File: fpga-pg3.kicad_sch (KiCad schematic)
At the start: 20 parts, among them U1 XC7A35T-FGG484

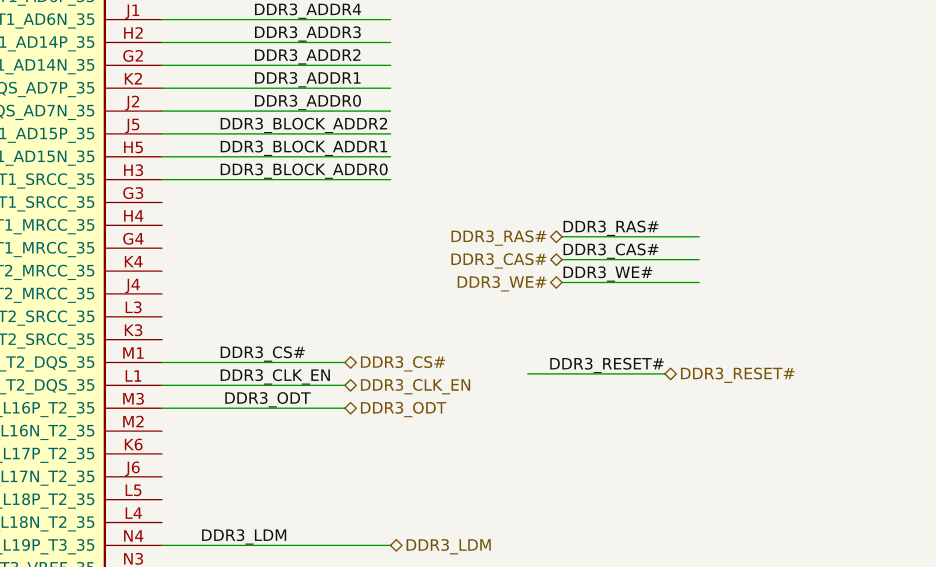
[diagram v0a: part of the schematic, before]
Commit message: filled out back connector, finished ddr pinning according to vivado
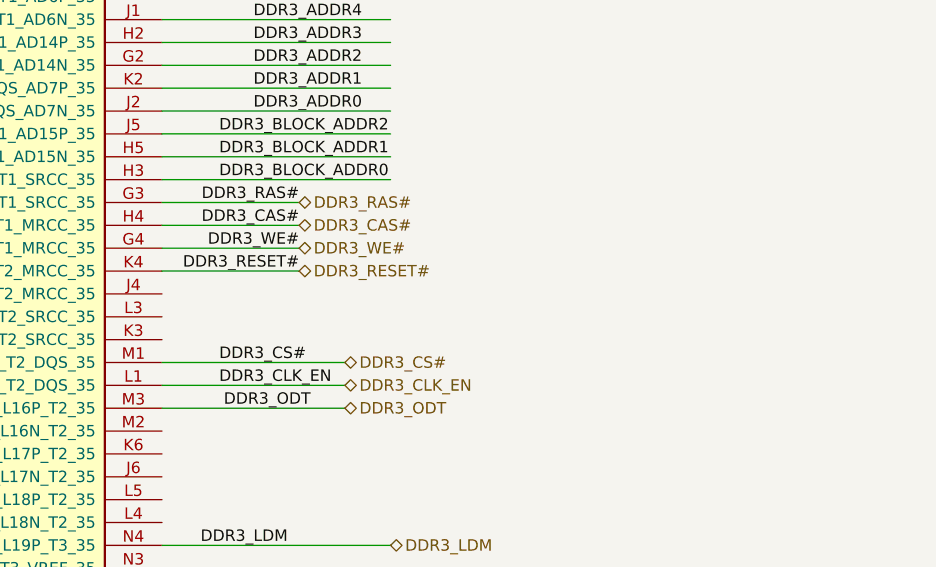
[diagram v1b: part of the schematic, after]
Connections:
- net DDR3_CAS#: now also U1.H4 (IO_L12P_T1_MRCC_35)
- net DDR3_RAS#: now also U1.G3 (IO_L11N_T1_SRCC_35)
- net DDR3_RESET#: now also U1.K4 (IO_L13P_T2_MRCC_35)
- net DDR3_WE#: now also U1.G4 (IO_L12N_T1_MRCC_35)
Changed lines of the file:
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@@
 	(wire
 		(pts
-			(xy 299.72 146.05) (xy 314.96 146.05)
+			(xy 270.51 142.24) (xy 255.27 142.24)
 		)
 		(stroke
@@
 	(wire
 		(pts
-			(xy 299.72 148.59) (xy 314.96 148.59)
-		)
-		(stroke
-			(width 0)
-			(type default)
-		)
-	)
-	(wire
-		(pts
-			(xy 299.72 151.13) (xy 314.96 151.13)
+			(xy 270.51 144.78) (xy 255.27 144.78)
+		)
+		(stroke
+			(width 0)
+			(type default)
+		)
+	)
+	(wire
+		(pts
+			(xy 270.51 147.32) (xy 255.27 147.32)
 		)
 		(stroke
@@
 	(wire
 		(pts
-			(xy 311.15 161.29) (xy 295.91 161.29)
+			(xy 270.51 149.86) (xy 255.27 149.86)
 		)
 		(stroke
@@
 	)
 	(label "DDR3_RAS#"
-		(at 299.72 146.05 0)
-		(effects
-			(font
-				(size 1.27 1.27)
-			)
-			(justify left bottom)
+		(at 270.51 142.24 180)
+		(effects
+			(font
+				(size 1.27 1.27)
+			)
+			(justify right bottom)
 		)
 	)
@@
 	)
 	(label "DDR3_WE#"
-		(at 299.72 151.13 0)
-		(effects
-			(font
-				(size 1.27 1.27)
-			)
-			(justify left bottom)
+		(at 270.51 147.32 180)
+		(effects
+			(font
+				(size 1.27 1.27)
+			)
+			(justify right bottom)
 		)
 	)
@@
 	)
 	(label "DDR3_CAS#"
-		(at 299.72 148.59 0)
-		(effects
-			(font
-				(size 1.27 1.27)
-			)
-			(justify left bottom)
+		(at 270.51 144.78 180)
+		(effects
+			(font
+				(size 1.27 1.27)
+			)
+			(justify right bottom)
 		)
 	)
@@
 	)
 	(label "DDR3_RESET#"
-		(at 311.15 161.29 180)
+		(at 270.51 149.86 180)
 		(effects
 			(font
@@
 	(hierarchical_label "DDR3_RESET#"
 		(shape bidirectional)
-		(at 311.15 161.29 0)
+		(at 270.51 149.86 0)
 		(effects
 			(font
@@
 	(hierarchical_label "DDR3_WE#"
 		(shape bidirectional)
-		(at 299.72 151.13 180)
-		(effects
-			(font
-				(size 1.27 1.27)
-			)
-			(justify right)
+		(at 270.51 147.32 0)
+		(effects
+			(font
+				(size 1.27 1.27)
+			)
+			(justify left)
 		)
 	)
@@
 	(hierarchical_label "DDR3_CAS#"
 		(shape bidirectional)
-		(at 299.72 148.59 180)
-		(effects
-			(font
-				(size 1.27 1.27)
-			)
-			(justify right)
+		(at 270.51 144.78 0)
+		(effects
+			(font
+				(size 1.27 1.27)
+			)
+			(justify left)
 		)
 	)
 	(hierarchical_label "DDR3_RAS#"
 		(shape bidirectional)
-		(at 299.72 146.05 180)
-		(effects
-			(font
-				(size 1.27 1.27)
-			)
-			(justify right)
-		)
-	)
+		(at 270.51 142.24 0)
+		(effects
+			(font
+				(size 1.27 1.27)
+			)
+			(justify left)
+		)
+	)

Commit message: added a lot of stuff
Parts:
- renumbered C72 to C29, C73 to C30, C74 to C31, C75 to C32, C76 to C33, C77 to C34, C78 to C35, C79 to C36, C80 to C37, C81 to C38, C82 to C39, C83 to C40, C84 to C41, C85 to C42, R11 to R1, R12 to R2, R13 to R3, R14 to R4, R15 to R5
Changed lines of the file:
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@@
 		(on_board yes)
 		(dnp no)
-		(property "Reference" "C73"
+		(property "Reference" "C30"
 			(at 91.44 52.0699 0)
 			(effects
@@
 			(project "logix-core"
 				(path "/cf3b7c5f-6ddc-4e3f-9529-0bcf5eec6f23/824409ff-e0aa-4944-ad80-228eadb659f9/9208eeea-aa23-4f0a-a0f4-52abaf751fbe"
-					(reference "C73")
+					(reference "C30")
 					(unit 1)
 				)
@@
 		(dnp no)
 		(fields_autoplaced yes)
-		(property "Reference" "C78"
+		(property "Reference" "C35"
 			(at 154.94 52.0699 0)
 			(effects
@@
 			(project "logix-core"
 				(path "/cf3b7c5f-6ddc-4e3f-9529-0bcf5eec6f23/824409ff-e0aa-4944-ad80-228eadb659f9/9208eeea-aa23-4f0a-a0f4-52abaf751fbe"
-					(reference "C78")
+					(reference "C35")
 					(unit 1)
 				)
@@
 		(dnp no)
 		(fields_autoplaced yes)
-		(property "Reference" "C75"
+		(property "Reference" "C32"
 			(at 116.84 52.0699 0)
 			(effects
@@
 			(project "logix-core"
 				(path "/cf3b7c5f-6ddc-4e3f-9529-0bcf5eec6f23/824409ff-e0aa-4944-ad80-228eadb659f9/9208eeea-aa23-4f0a-a0f4-52abaf751fbe"
-					(reference "C75")
+					(reference "C32")
 					(unit 1)
 				)
@@
 		(on_board yes)
 		(dnp no)
-		(property "Reference" "R15"
+		(property "Reference" "R5"
 			(at -90.424 94.488 90)
 			(effects
@@
 			(project "logix-core"
 				(path "/cf3b7c5f-6ddc-4e3f-9529-0bcf5eec6f23/824409ff-e0aa-4944-ad80-228eadb659f9/9208eeea-aa23-4f0a-a0f4-52abaf751fbe"
-					(reference "R15")
+					(reference "R5")
 					(unit 1)
 				)
@@
 		(on_board yes)
 		(dnp no)
-		(property "Reference" "R11"
+		(property "Reference" "R1"
 			(at -90.424 69.088 90)
 			(effects
@@
 			(project "logix-core"
 				(path "/cf3b7c5f-6ddc-4e3f-9529-0bcf5eec6f23/824409ff-e0aa-4944-ad80-228eadb659f9/9208eeea-aa23-4f0a-a0f4-52abaf751fbe"
-					(reference "R11")
+					(reference "R1")
 					(unit 1)
 				)
@@
 		(on_board yes)
 		(dnp no)
-		(property "Reference" "R13"
+		(property "Reference" "R3"
 			(at -90.424 74.168 90)
 			(effects
@@
 			(project "logix-core"
 				(path "/cf3b7c5f-6ddc-4e3f-9529-0bcf5eec6f23/824409ff-e0aa-4944-ad80-228eadb659f9/9208eeea-aa23-4f0a-a0f4-52abaf751fbe"
-					(reference "R13")
+					(reference "R3")
 					(unit 1)
 				)
@@
 		(on_board yes)
 		(dnp no)
-		(property "Reference" "R14"
+		(property "Reference" "R4"
 			(at -90.424 76.708 90)
 			(effects
@@
 			(project "logix-core"
 				(path "/cf3b7c5f-6ddc-4e3f-9529-0bcf5eec6f23/824409ff-e0aa-4944-ad80-228eadb659f9/9208eeea-aa23-4f0a-a0f4-52abaf751fbe"
-					(reference "R14")
+					(reference "R4")
 					(unit 1)
 				)
@@
 		(dnp no)
 		(fields_autoplaced yes)
-		(property "Reference" "C76"
+		(property "Reference" "C33"
 			(at 129.54 52.0699 0)
 			(effects
@@
 			(project "logix-core"
 				(path "/cf3b7c5f-6ddc-4e3f-9529-0bcf5eec6f23/824409ff-e0aa-4944-ad80-228eadb659f9/9208eeea-aa23-4f0a-a0f4-52abaf751fbe"
-					(reference "C76")
+					(reference "C33")
 					(unit 1)
 				)
@@
 		(dnp no)
 		(fields_autoplaced yes)
-		(property "Reference" "C77"
+		(property "Reference" "C34"
 			(at 142.24 52.0699 0)
 			(effects
@@
 			(project "logix-core"
 				(path "/cf3b7c5f-6ddc-4e3f-9529-0bcf5eec6f23/824409ff-e0aa-4944-ad80-228eadb659f9/9208eeea-aa23-4f0a-a0f4-52abaf751fbe"
-					(reference "C77")
+					(reference "C34")
 					(unit 1)
 				)
@@
 		(dnp no)
 		(fields_autoplaced yes)
-		(property "Reference" "#PWR071"
+		(property "Reference" "#PWR06"
 			(at 327.66 68.58 0)
 			(effects
@@
 			(project "logix-core"
 				(path "/cf3b7c5f-6ddc-4e3f-9529-0bcf5eec6f23/824409ff-e0aa-4944-ad80-228eadb659f9/9208eeea-aa23-4f0a-a0f4-52abaf751fbe"
-					(reference "#PWR071")
+					(reference "#PWR06")
 					(unit 1)
 				)
@@
 		(on_board yes)
 		(dnp no)
-		(property "Reference" "C84"
+		(property "Reference" "C41"
 			(at 317.5 52.0699 0)
 			(effects
@@
 			(project "logix-core"
 				(path "/cf3b7c5f-6ddc-4e3f-9529-0bcf5eec6f23/824409ff-e0aa-4944-ad80-228eadb659f9/9208eeea-aa23-4f0a-a0f4-52abaf751fbe"
-					(reference "C84")
+					(reference "C41")
 					(unit 1)
 				)
@@
 		(dnp no)
 		(fields_autoplaced yes)
-		(property "Reference" "C82"
+		(property "Reference" "C39"
 			(at 292.1 52.0699 0)
 			(effects
@@
 			(project "logix-core"
 				(path "/cf3b7c5f-6ddc-4e3f-9529-0bcf5eec6f23/824409ff-e0aa-4944-ad80-228eadb659f9/9208eeea-aa23-4f0a-a0f4-52abaf751fbe"
-					(reference "C82")
+					(reference "C39")
 					(unit 1)
 				)
@@
 		(dnp no)
 		(fields_autoplaced yes)
-		(property "Reference" "#PWR070"
+		(property "Reference" "#PWR05"
 			(at 81.28 68.58 0)
 			(effects
@@
 			(project "logix-core"
 				(path "/cf3b7c5f-6ddc-4e3f-9529-0bcf5eec6f23/824409ff-e0aa-4944-ad80-228eadb659f9/9208eeea-aa23-4f0a-a0f4-52abaf751fbe"
-					(reference "#PWR070")
+					(reference "#PWR05")
 					(unit 1)
 				)
@@
 		(dnp no)
 		(fields_autoplaced yes)
-		(property "Reference" "C80"
+		(property "Reference" "C37"
 			(at 266.7 52.0699 0)
 			(effects
@@
 			(project "logix-core"
 				(path "/cf3b7c5f-6ddc-4e3f-9529-0bcf5eec6f23/824409ff-e0aa-4944-ad80-228eadb659f9/9208eeea-aa23-4f0a-a0f4-52abaf751fbe"
-					(reference "C80")
+					(reference "C37")
 					(unit 1)
 				)
@@
 		(dnp no)
 		(fields_autoplaced yes)
-		(property "Reference" "C85"
+		(property "Reference" "C42"
 			(at 330.2 52.0699 0)
 			(effects
@@
 			(project "logix-core"
 				(path "/cf3b7c5f-6ddc-4e3f-9529-0bcf5eec6f23/824409ff-e0aa-4944-ad80-228eadb659f9/9208eeea-aa23-4f0a-a0f4-52abaf751fbe"
-					(reference "C85")
+					(reference "C42")
 					(unit 1)
 				)
@@
 		(dnp no)
 		(fields_autoplaced yes)
-		(property "Reference" "C74"
+		(property "Reference" "C31"
 			(at 104.14 52.0699 0)
 			(effects
@@
 			(project "logix-core"
 				(path "/cf3b7c5f-6ddc-4e3f-9529-0bcf5eec6f23/824409ff-e0aa-4944-ad80-228eadb659f9/9208eeea-aa23-4f0a-a0f4-52abaf751fbe"
-					(reference "C74")
+					(reference "C31")
 					(unit 1)
 				)
@@
 		(dnp no)
 		(fields_autoplaced yes)
-		(property "Reference" "C83"
+		(property "Reference" "C40"
 			(at 304.8 52.0699 0)
 			(effects
@@
 			(project "logix-core"
 				(path "/cf3b7c5f-6ddc-4e3f-9529-0bcf5eec6f23/824409ff-e0aa-4944-ad80-228eadb659f9/9208eeea-aa23-4f0a-a0f4-52abaf751fbe"
-					(reference "C83")
+					(reference "C40")
 					(unit 1)
 				)
@@
 		(dnp no)
 		(fields_autoplaced yes)
-		(property "Reference" "C79"
+		(property "Reference" "C36"
 			(at 254 52.0699 0)
 			(effects
@@
 			(project "logix-core"
 				(path "/cf3b7c5f-6ddc-4e3f-9529-0bcf5eec6f23/824409ff-e0aa-4944-ad80-228eadb659f9/9208eeea-aa23-4f0a-a0f4-52abaf751fbe"
-					(reference "C79")
+					(reference "C36")
 					(unit 1)
 				)
@@
 		(dnp no)
 		(fields_autoplaced yes)
-		(property "Reference" "C81"
+		(property "Reference" "C38"
 			(at 279.4 52.0699 0)
 			(effects
@@
 			(project "logix-core"
 				(path "/cf3b7c5f-6ddc-4e3f-9529-0bcf5eec6f23/824409ff-e0aa-4944-ad80-228eadb659f9/9208eeea-aa23-4f0a-a0f4-52abaf751fbe"
-					(reference "C81")
+					(reference "C38")
 					(unit 1)
 				)
@@
 		(dnp no)
 		(fields_autoplaced yes)
-		(property "Reference" "C72"
+		(property "Reference" "C29"
 			(at 78.74 52.0699 0)
 			(effects
@@
 			(project "logix-core"
 				(path "/cf3b7c5f-6ddc-4e3f-9529-0bcf5eec6f23/824409ff-e0aa-4944-ad80-228eadb659f9/9208eeea-aa23-4f0a-a0f4-52abaf751fbe"
-					(reference "C72")
+					(reference "C29")
 					(unit 1)
 				)
@@
 		(on_board yes)
 		(dnp no)
-		(property "Reference" "R12"
+		(property "Reference" "R2"
 			(at -90.424 71.628 90)
 			(effects
@@
 			(project "logix-core"
 				(path "/cf3b7c5f-6ddc-4e3f-9529-0bcf5eec6f23/824409ff-e0aa-4944-ad80-228eadb659f9/9208eeea-aa23-4f0a-a0f4-52abaf751fbe"
-					(reference "R12")
+					(reference "R2")
 					(unit 1)
 				)

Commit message: did alot of stuff
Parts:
- C29, C42: footprint Capacitor_SMD:C_1210_3225Metric -> Capacitor_SMD:C_1206_3216Metric; LCSC (none) -> C96123
- C30, C31, C40, C41: LCSC (none) -> C23733
- C32, C33, C34, C35, C36, C37, C38, C39: LCSC (none) -> C47339
- R1, R2, R3, R4, R5: footprint Resistor_SMD:R_0402_1005Metric_Pad0.72x0.64mm_HandSolder -> Resistor_SMD:R_0402_1005Metric; LCSC C226391 -> C17168
- U1: LCSC (none) -> C1521727
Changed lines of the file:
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@@
+			)
+		)
+		(property "LCSC" "C23733"
+			(at 87.63 53.34 0)
+			(effects
+				(font
+					(size 1.27 1.27)
+				)
 			)
 		)
@@
 			)
 		)
+		(property "LCSC" "C47339"
+			(at 151.13 53.34 0)
+			(effects
+				(font
+					(size 1.27 1.27)
+				)
+			)
+		)
 		(pin "2"
 		)
@@
 			)
 		)
+		(property "LCSC" "C47339"
+			(at 113.03 53.34 0)
+			(effects
+				(font
+					(size 1.27 1.27)
+				)
+			)
+		)
 		(pin "2"
 		)
@@
 			)
 		)
-		(property "Footprint" "Resistor_SMD:R_0402_1005Metric_Pad0.72x0.64mm_HandSolder"
+		(property "Footprint" "Resistor_SMD:R_0402_1005Metric"
 			(at -85.09 97.028 90)
 			(effects
@@
 			)
 		)
-		(property "LCSC" "C226391"
+		(property "LCSC" "C17168"
 			(at -85.09 95.25 0)
 			(effects
@@
 			)
 		)
-		(property "Footprint" "Resistor_SMD:R_0402_1005Metric_Pad0.72x0.64mm_HandSolder"
+		(property "Footprint" "Resistor_SMD:R_0402_1005Metric"
 			(at -85.09 71.628 90)
 			(effects
@@
 			)
 		)
-		(property "LCSC" "C226391"
+		(property "LCSC" "C17168"
 			(at -85.09 69.85 0)
 			(effects
@@
 			)
 		)
-		(property "Footprint" "Resistor_SMD:R_0402_1005Metric_Pad0.72x0.64mm_HandSolder"
+		(property "Footprint" "Resistor_SMD:R_0402_1005Metric"
 			(at -85.09 76.708 90)
 			(effects
@@
 			)
 		)
-		(property "LCSC" "C226391"
+		(property "LCSC" "C17168"
 			(at -85.09 74.93 0)
 			(effects
@@
 			)
 		)
-		(property "Footprint" "Resistor_SMD:R_0402_1005Metric_Pad0.72x0.64mm_HandSolder"
+		(property "Footprint" "Resistor_SMD:R_0402_1005Metric"
 			(at -85.09 79.248 90)
 			(effects
@@
 			)
 		)
-		(property "LCSC" "C226391"
+		(property "LCSC" "C17168"
 			(at -85.09 77.47 0)
 			(effects
@@
 			)
 		)
+		(property "LCSC" "C47339"
+			(at 125.73 53.34 0)
+			(effects
+				(font
+					(size 1.27 1.27)
+				)
+			)
+		)
 		(pin "2"
 		)
@@
 				)
 				(hide yes)
+			)
+		)
+		(property "LCSC" "C47339"
+			(at 138.43 53.34 0)
+			(effects
+				(font
+					(size 1.27 1.27)
+				)
 			)
 		)
@@
 			)
 		)
+		(property "LCSC" "C23733"
+			(at 321.31 53.34 0)
+			(effects
+				(font
+					(size 1.27 1.27)
+				)
+			)
+		)
 		(pin "2"
 		)
@@
 			)
 		)
+		(property "LCSC" "C47339"
+			(at 295.91 53.34 0)
+			(effects
+				(font
+					(size 1.27 1.27)
+				)
+			)
+		)
 		(pin "2"
 		)
@@
 			)
 		)
+		(property "LCSC" "C47339"
+			(at 270.51 53.34 0)
+			(effects
+				(font
+					(size 1.27 1.27)
+				)
+			)
+		)
 		(pin "2"
 		)
@@
 			)
 		)
-		(property "Footprint" "Capacitor_SMD:C_1210_3225Metric"
+		(property "Footprint" "Capacitor_SMD:C_1206_3216Metric"
 			(at 333.0448 57.15 0)
 			(effects
@@
 				)
 				(hide yes)
+			)
+		)
+		(property "LCSC" "C96123"
+			(at 334.01 53.34 0)
+			(effects
+				(font
+					(size 1.27 1.27)
+				)
 			)
 		)
@@
 			)
 		)
+		(property "LCSC" "C23733"
+			(at 100.33 53.34 0)
+			(effects
+				(font
+					(size 1.27 1.27)
+				)
+			)
+		)
 		(pin "2"
 		)
@@
 				)
 				(hide yes)
+			)
+		)
+		(property "LCSC" "C1521727"
+			(at 204.47 139.7 0)
+			(effects
+				(font
+					(size 1.27 1.27)
+				)
 			)
 		)
@@
 			)
 		)
+		(property "LCSC" "C23733"
+			(at 308.61 53.34 0)
+			(effects
+				(font
+					(size 1.27 1.27)
+				)
+			)
+		)
 		(pin "2"
 		)
@@
 			)
 		)
+		(property "LCSC" "C47339"
+			(at 257.81 53.34 0)
+			(effects
+				(font
+					(size 1.27 1.27)
+				)
+			)
+		)
 		(pin "2"
 		)
@@
 			)
 		)
+		(property "LCSC" "C47339"
+			(at 283.21 53.34 0)
+			(effects
+				(font
+					(size 1.27 1.27)
+				)
+			)
+		)
 		(pin "2"
 		)
@@
 			)
 		)
-		(property "Footprint" "Capacitor_SMD:C_1210_3225Metric"
+		(property "Footprint" "Capacitor_SMD:C_1206_3216Metric"
 			(at 75.8952 57.15 0)
 			(effects
@@
 				)
 				(hide yes)
+			)
+		)
+		(property "LCSC" "C96123"
+			(at 74.93 53.34 0)
+			(effects
+				(font
+					(size 1.27 1.27)
+				)
 			)
 		)
@@
 			)
 		)
-		(property "Footprint" "Resistor_SMD:R_0402_1005Metric_Pad0.72x0.64mm_HandSolder"
+		(property "Footprint" "Resistor_SMD:R_0402_1005Metric"
 			(at -85.09 74.168 90)
 			(effects
@@
 			)
 		)
-		(property "LCSC" "C226391"
+		(property "LCSC" "C17168"
 			(at -85.09 72.39 0)
 			(effects
